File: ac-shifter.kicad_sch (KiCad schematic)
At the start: 11 parts

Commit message: schem: annotate back ac level shifter page
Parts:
- gave numbers to parts that had none: 6
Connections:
- net +10/20DC: now also U10.8 (V+)
- net GND: now also U10.4 (V-)
- net OL: now also U10.7; no longer U10.1
- net Vref: now also U10.6 (-); no longer U10.2 (-)
- net at C32.1, R37.2, R47.1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: now also U10.5 (+); no longer U10.3 (+)
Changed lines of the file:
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@@
 		(dnp no)
 		(fields_autoplaced yes)
-		(property "Reference" "R?"
+		(property "Reference" "R48"
 			(at 184.15 105.4099 0)
 			(effects
@@
 			(project "esp32c6-sensor-devboard"
 				(path "/f6edeef8-7fa0-4f55-9ad8-145372f41e3e/b7a168fa-ef36-46f7-85e2-013385835bc1"
-					(reference "R?")
+					(reference "R48")
 					(unit 1)
 				)
@@
 		(lib_id "Comparator:LM393")
 		(at 128.27 60.96 0)
-		(unit 1)
-		(exclude_from_sim no)
-		(in_bom yes)
-		(on_board yes)
-		(dnp no)
-		(fields_autoplaced yes)
-		(property "Reference" "U?"
+		(unit 3)
+		(exclude_from_sim no)
+		(in_bom yes)
+		(on_board yes)
+		(dnp no)
+		(fields_autoplaced yes)
+		(property "Reference" "U10"
 			(at 127 59.6899 0)
 			(effects
@@
 			(project "esp32c6-sensor-devboard"
 				(path "/f6edeef8-7fa0-4f55-9ad8-145372f41e3e/b7a168fa-ef36-46f7-85e2-013385835bc1"
-					(reference "U?")
-					(unit 1)
+					(reference "U10")
+					(unit 3)
 				)
 			)
@@
 		(on_board yes)
 		(dnp no)
-		(property "Reference" "C?"
+		(property "Reference" "C40"
 			(at 111.76 55.8799 0)
 			(effects
@@
 			(project "esp32c6-sensor-devboard"
 				(path "/f6edeef8-7fa0-4f55-9ad8-145372f41e3e/b7a168fa-ef36-46f7-85e2-013385835bc1"
-					(reference "C?")
+					(reference "C40")
 					(unit 1)
 				)
@@
 		(on_board yes)
 		(dnp no)
-		(property "Reference" "D?"
+		(property "Reference" "D5"
 			(at 99.568 90.424 0)
 			(effects
@@
 			(project "esp32c6-sensor-devboard"
 				(path "/f6edeef8-7fa0-4f55-9ad8-145372f41e3e/b7a168fa-ef36-46f7-85e2-013385835bc1"
-					(reference "D?")
+					(reference "D5")
 					(unit 1)
 				)
@@
 		(dnp no)
 		(fields_autoplaced yes)
-		(property "Reference" "C?"
+		(property "Reference" "C39"
 			(at 113.03 99.0599 0)
 			(effects
@@
 			(project "esp32c6-sensor-devboard"
 				(path "/f6edeef8-7fa0-4f55-9ad8-145372f41e3e/b7a168fa-ef36-46f7-85e2-013385835bc1"
-					(reference "C?")
+					(reference "C39")
 					(unit 1)
 				)
@@
 		(on_board yes)
 		(dnp no)
-		(property "Reference" "U?"
+		(property "Reference" "U10"
 			(at 170.18 68.58 0)
 			(effects
@@
 			(project "esp32c6-sensor-devboard"
 				(path "/f6edeef8-7fa0-4f55-9ad8-145372f41e3e/b7a168fa-ef36-46f7-85e2-013385835bc1"
-					(reference "U?")
+					(reference "U10")
 					(unit 1)
 				)
@@
 		(dnp no)
 		(fields_autoplaced yes)
-		(property "Reference" "R?"
+		(property "Reference" "R47"
 			(at 142.24 99.0599 0)
 			(effects
@@
 			(project "esp32c6-sensor-devboard"
 				(path "/f6edeef8-7fa0-4f55-9ad8-145372f41e3e/b7a168fa-ef36-46f7-85e2-013385835bc1"
-					(reference "R?")
+					(reference "R47")
 					(unit 1)
 				)
@@
 		(lib_id "Comparator:LM393")
 		(at 170.18 114.3 0)
-		(unit 1)
-		(exclude_from_sim no)
-		(in_bom yes)
-		(on_board yes)
-		(dnp no)
-		(fields_autoplaced yes)
-		(property "Reference" "U?"
+		(unit 2)
+		(exclude_from_sim no)
+		(in_bom yes)
+		(on_board yes)
+		(dnp no)
+		(fields_autoplaced yes)
+		(property "Reference" "U10"
 			(at 170.18 104.14 0)
 			(effects
@@
 			(project "esp32c6-sensor-devboard"
 				(path "/f6edeef8-7fa0-4f55-9ad8-145372f41e3e/b7a168fa-ef36-46f7-85e2-013385835bc1"
-					(reference "U?")
-					(unit 1)
-				)
-			)
+					(reference "U10")
+					(unit 2)
+				)
+			)

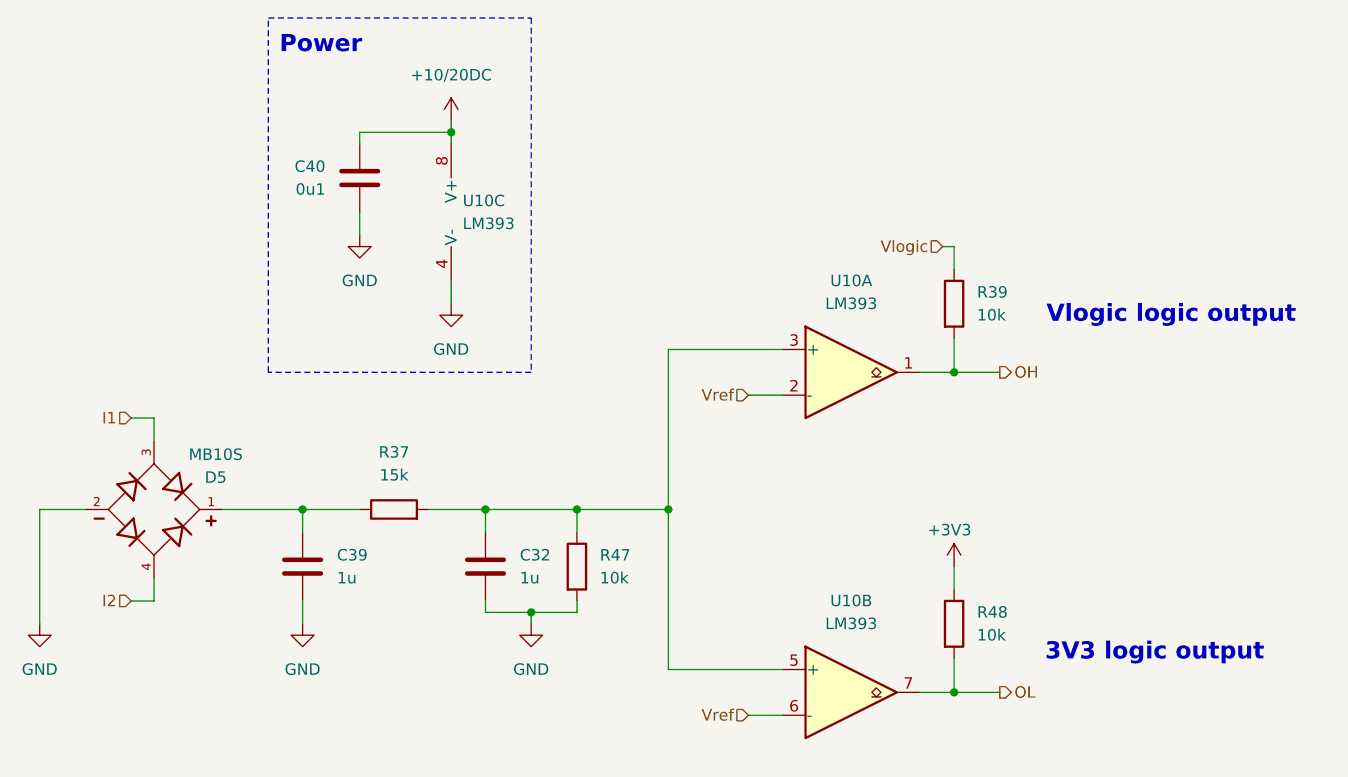
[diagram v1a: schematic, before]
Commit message: schem: add 3CH 24V/12V Input level shifter
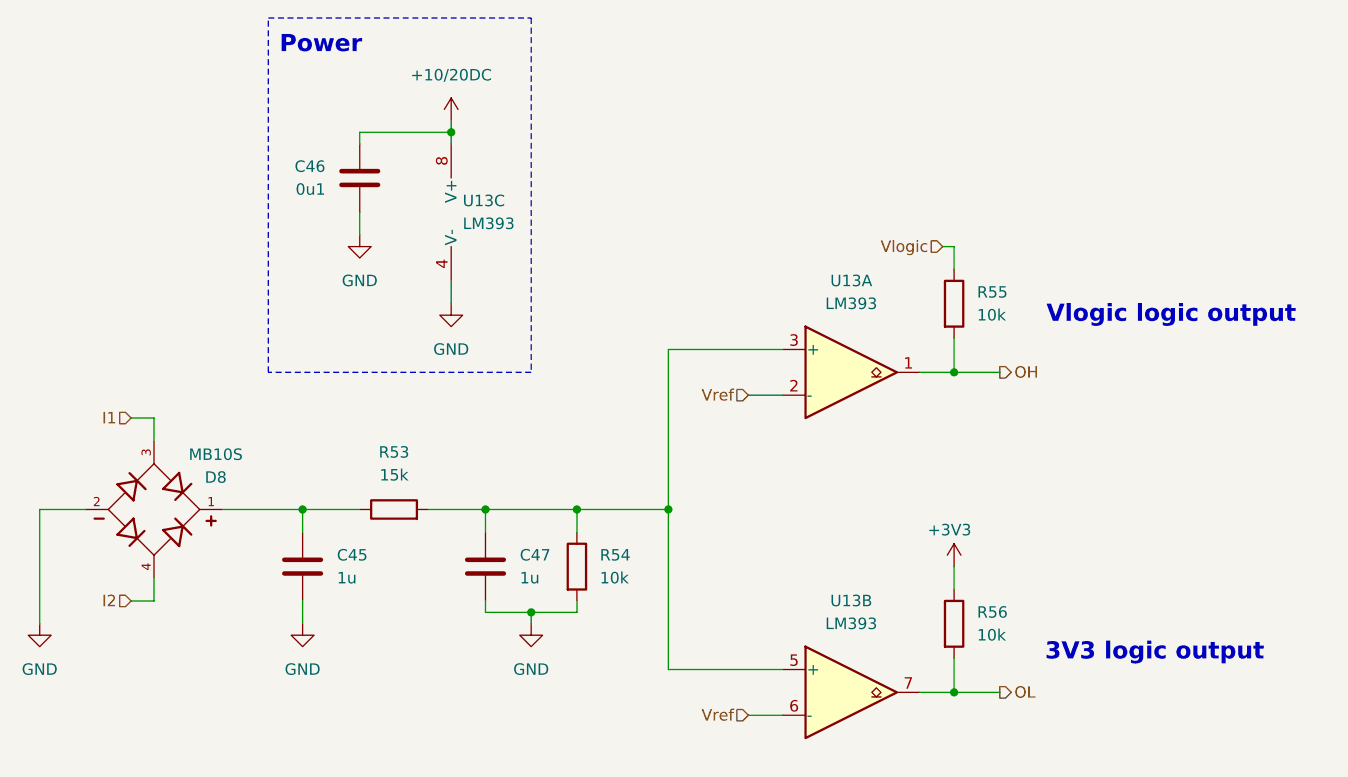
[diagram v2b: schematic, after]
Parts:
- renumbered C39 to C45, C40 to C46, C32 to C47, D5 to D8, R37 to R53, R47 to R54, R39 to R55, R48 to R56, U10 to U13

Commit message: schem: add comparator test points
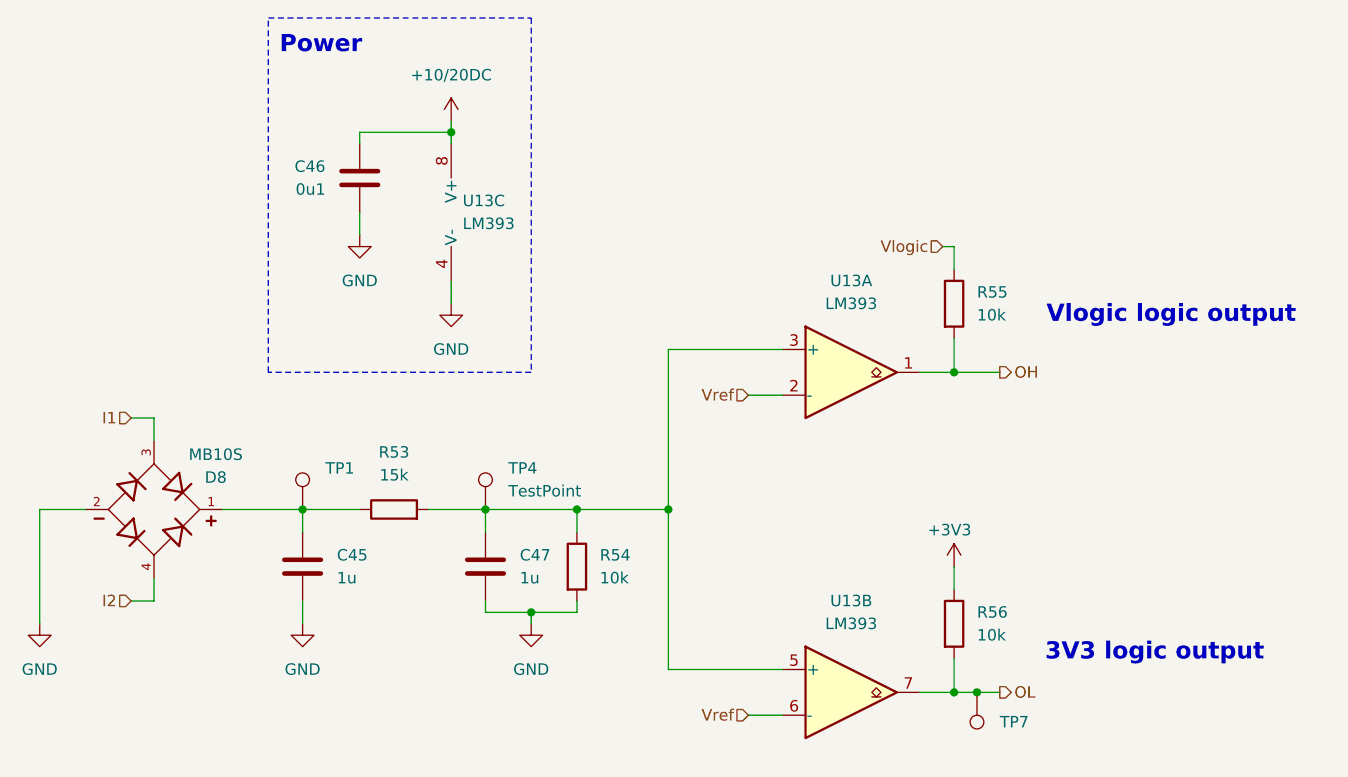
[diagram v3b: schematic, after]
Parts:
- added TP1, TP4, TP7: TestPoint, symbol Connector:TestPoint
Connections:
- net OL: now also TP7.1
- net at C45.1, D8.1, R53.1: now also TP1.1
- net at C47.1, R53.2, R54.1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: now also TP4.1
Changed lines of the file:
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@@
+	)
+	(junction
+		(at 184.15 114.3)
+		(diameter 0)
+		(color 0 0 0 0)
 	)
 	(junction
@@
 	(wire
 		(pts
-			(xy 181.61 114.3) (xy 186.69 114.3)
+			(xy 181.61 114.3) (xy 184.15 114.3)
 		)
 		(stroke
@@
 		(pts
 			(xy 181.61 74.93) (xy 181.61 78.74)
+		)
+		(stroke
+			(width 0)
+			(type default)
+		)
+	)
+	(wire
+		(pts
+			(xy 184.15 114.3) (xy 186.69 114.3)
 		)
 		(stroke
@@
 	)
 	(symbol
+		(lib_id "Connector:TestPoint")
+		(at 129.54 93.98 0)
+		(unit 1)
+		(exclude_from_sim no)
+		(in_bom yes)
+		(on_board yes)
+		(dnp no)
+		(fields_autoplaced yes)
+		(property "Reference" "TP4"
+			(at 132.08 89.4079 0)
+			(effects
+				(font
+					(size 1.27 1.27)
+				)
+				(justify left)
+			)
+		)
+		(property "Value" "TestPoint"
+			(at 132.08 91.9479 0)
+			(effects
+				(font
+					(size 1.27 1.27)
+				)
+				(justify left)
+			)
+		)
+		(property "Footprint" ""
+			(at 134.62 93.98 0)
+			(effects
+				(font
+					(size 1.27 1.27)
+				)
+				(hide yes)
+			)
+		)
+		(property "Datasheet" "~"
+			(at 134.62 93.98 0)
+			(effects
+				(font
+					(size 1.27 1.27)
+				)
+				(hide yes)
+			)
+		)
+		(property "Description" "test point"
+			(at 129.54 93.98 0)
+			(effects
+				(font
+					(size 1.27 1.27)
+				)
+				(hide yes)
+			)
+		)
+		(pin "1"
+		)
+		(instances
+			(project ""
+				(path "/f6edeef8-7fa0-4f55-9ad8-145372f41e3e/30405a70-5ee8-4fa0-855b-2b8bdab4954c"
+					(reference "TP5")
+					(unit 1)
+				)
+				(path "/f6edeef8-7fa0-4f55-9ad8-145372f41e3e/5f6c93b9-e933-4ea9-a357-6909cb7c1eb6"
+					(reference "TP4")
+					(unit 1)
+				)
+				(path "/f6edeef8-7fa0-4f55-9ad8-145372f41e3e/a6afd72b-5a4f-47cb-8cd9-76696d192618"
+					(reference "TP6")
+					(unit 1)
+				)
+			)
+		)
+	)
+	(symbol
 		(lib_id "Device:C")
 		(at 129.54 100.33 0)
@@
 	)
 	(symbol
+		(lib_id "Connector:TestPoint")
+		(at 109.22 93.98 0)
+		(unit 1)
+		(exclude_from_sim no)
+		(in_bom yes)
+		(on_board yes)
+		(dnp no)
+		(fields_autoplaced yes)
+		(property "Reference" "TP1"
+			(at 111.76 89.4079 0)
+			(effects
+				(font
+					(size 1.27 1.27)
+				)
+				(justify left)
+			)
+		)
+		(property "Value" "TestPoint"
+			(at 111.76 91.9479 0)
+			(effects
+				(font
+					(size 1.27 1.27)
+				)
+				(justify left)
+				(hide yes)
+			)
+		)
+		(property "Footprint" ""
+			(at 114.3 93.98 0)
+			(effects
+				(font
+					(size 1.27 1.27)
+				)
+				(hide yes)
+			)
+		)
+		(property "Datasheet" "~"
+			(at 114.3 93.98 0)
+			(effects
+				(font
+					(size 1.27 1.27)
+				)
+				(hide yes)
+			)
+		)
+		(property "Description" "test point"
+			(at 109.22 93.98 0)
+			(effects
+				(font
+					(size 1.27 1.27)
+				)
+				(hide yes)
+			)
+		)
+		(pin "1"
+		)
+		(instances
+			(project ""
+				(path "/f6edeef8-7fa0-4f55-9ad8-145372f41e3e/30405a70-5ee8-4fa0-855b-2b8bdab4954c"
+					(reference "TP2")
+					(unit 1)
+				)
+				(path "/f6edeef8-7fa0-4f55-9ad8-145372f41e3e/5f6c93b9-e933-4ea9-a357-6909cb7c1eb6"
+					(reference "TP1")
+					(unit 1)
+				)
+				(path "/f6edeef8-7fa0-4f55-9ad8-145372f41e3e/a6afd72b-5a4f-47cb-8cd9-76696d192618"
+					(reference "TP3")
+					(unit 1)
+				)
+			)
+		)
+	)
+	(symbol
 		(lib_id "Device:R")
 		(at 181.61 71.12 0)
@@
 				)
 			)
+		)
+	)
+	(symbol
+		(lib_id "Connector:TestPoint")
+		(at 184.15 114.3 180)
+		(unit 1)
+		(exclude_from_sim no)
+		(in_bom yes)
+		(on_board yes)
+		(dnp no)
+		(fields_autoplaced yes)
+		(property "Reference" "TP7"
+			(at 186.69 117.6019 0)
+			(effects
+				(font
+					(size 1.27 1.27)
+				)
+				(justify right)
+			)
+		)
+		(property "Value" "TestPoint"
+			(at 181.61 116.3321 0)
+			(effects
+				(font
+					(size 1.27 1.27)
+				)
+				(justify left)
+				(hide yes)
+			)
+		)
+		(property "Footprint" ""
+			(at 179.07 114.3 0)
+			(effects
+				(font
+					(size 1.27 1.27)
+				)
+				(hide yes)
+			)
+		)
+		(property "Datasheet" "~"
+			(at 179.07 114.3 0)
+			(effects
+				(font
+					(size 1.27 1.27)
+				)
+				(hide yes)
+			)
+		)
+		(property "Description" "test point"
+			(at 184.15 114.3 0)
+			(effects
+				(font
+					(size 1.27 1.27)
+				)
+				(hide yes)
+			)
+		)
+		(pin "1"
+		)
+		(instances
+			(project "esp32c6-sensor-devboard"
+				(path "/f6edeef8-7fa0-4f55-9ad8-145372f41e3e/30405a70-5ee8-4fa0-855b-2b8bdab4954c"
+					(reference "TP8")
+					(unit 1)
+				)
+				(path "/f6edeef8-7fa0-4f55-9ad8-145372f41e3e/5f6c93b9-e933-4ea9-a357-6909cb7c1eb6"
+					(reference "TP7")
+					(unit 1)
+				)
+				(path "/f6edeef8-7fa0-4f55-9ad8-145372f41e3e/a6afd72b-5a4f-47cb-8cd9-76696d192618"
+					(reference "TP9")
+					(unit 1)
+				)
+			)

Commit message: schem: add power test points
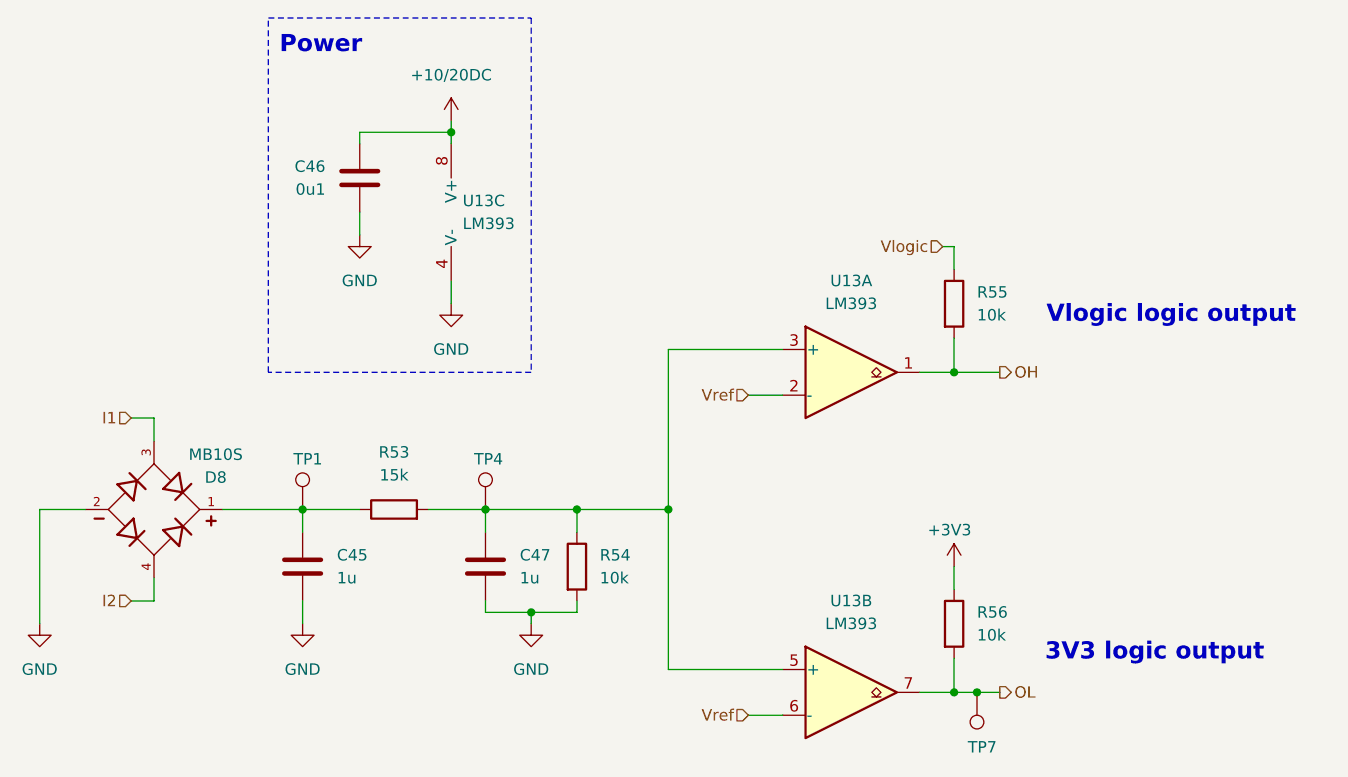
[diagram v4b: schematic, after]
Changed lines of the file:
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@@
 		(on_board yes)
 		(dnp no)
-		(fields_autoplaced yes)
 		(property "Reference" "TP4"
-			(at 132.08 89.4079 0)
+			(at 128.27 88.392 0)
 			(effects
 				(font
@@
 				)
 				(justify left)
+				(hide yes)
 			)
 		)
@@
 		(on_board yes)
 		(dnp no)
-		(fields_autoplaced yes)
 		(property "Reference" "TP1"
-			(at 111.76 89.4079 0)
+			(at 108.204 88.392 0)
 			(effects
 				(font
@@
 		(on_board yes)
 		(dnp no)
-		(fields_autoplaced yes)
 		(property "Reference" "TP7"
-			(at 186.69 117.6019 0)
-			(effects
-				(font
+			(at 183.134 120.396 0)
+			(effects
+				(font

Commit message: schem: add sheet titles
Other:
- company: (none) -> Rémi Ait-Younes
- title: (none) -> AC Level Shifter
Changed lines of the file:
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@@
 	(generator_version "9.0")
 	(paper "A4")
+	(title_block
+		(title "AC Level Shifter")
+		(date "2025-09-26")
+		(rev "01")
+		(company "Rémi Ait-Younes")
+	)
 	(rectangle
 		(start 105.41 39.37)

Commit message: schem: assign footprints
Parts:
- C45: footprint (none) -> Capacitor_SMD:C_0603_1608Metric
- C46, C47: footprint (none) -> Capacitor_SMD:C_0402_1005Metric
- R53, R54, R55, R56: footprint (none) -> Resistor_SMD:R_0603_1608Metric
- TP1, TP4, TP7: footprint (none) -> TestPoint:TestPoint_Pad_D2.0mm
- U13: footprint (none) -> Package_SO:SOIC-8_3.9x4.9mm_P1.27mm
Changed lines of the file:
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@@
 			)
 		)
-		(property "Footprint" ""
+		(property "Footprint" "Resistor_SMD:R_0603_1608Metric"
 			(at 179.832 106.68 90)
 			(effects
@@
 			)
 		)
-		(property "Footprint" ""
+		(property "Footprint" "Resistor_SMD:R_0603_1608Metric"
 			(at 119.38 95.758 90)
 			(effects
@@
 			)
 		)
-		(property "Footprint" ""
+		(property "Footprint" "Package_SO:SOIC-8_3.9x4.9mm_P1.27mm"
 			(at 128.27 60.96 0)
 			(effects
@@
 			)
 		)
-		(property "Footprint" ""
+		(property "Footprint" "Capacitor_SMD:C_0402_1005Metric"
 			(at 116.5352 60.96 0)
 			(effects
@@
 			)
 		)
-		(property "Footprint" ""
+		(property "Footprint" "TestPoint:TestPoint_Pad_D2.0mm"
 			(at 134.62 93.98 0)
 			(effects
@@
 			)
 		)
-		(property "Footprint" ""
+		(property "Footprint" "Capacitor_SMD:C_0402_1005Metric"
 			(at 130.5052 104.14 0)
 			(effects
@@
 			)
 		)
-		(property "Footprint" ""
+		(property "Footprint" "Capacitor_SMD:C_0603_1608Metric"
 			(at 110.1852 104.14 0)
 			(effects
@@
 			)
 		)
-		(property "Footprint" ""
+		(property "Footprint" "Package_SO:SOIC-8_3.9x4.9mm_P1.27mm"
 			(at 170.18 78.74 0)
 			(effects
@@
 			)
 		)
-		(property "Footprint" ""
+		(property "Footprint" "Resistor_SMD:R_0603_1608Metric"
 			(at 137.922 100.33 90)
 			(effects
@@
 			)
 		)
-		(property "Footprint" ""
+		(property "Footprint" "TestPoint:TestPoint_Pad_D2.0mm"
 			(at 114.3 93.98 0)
 			(effects
@@
 			)
 		)
-		(property "Footprint" ""
+		(property "Footprint" "Resistor_SMD:R_0603_1608Metric"
 			(at 179.832 71.12 90)
 			(effects
@@
 			)
 		)
-		(property "Footprint" ""
+		(property "Footprint" "Package_SO:SOIC-8_3.9x4.9mm_P1.27mm"
 			(at 170.18 114.3 0)
 			(effects
@@
 			)
 		)
-		(property "Footprint" ""
+		(property "Footprint" "TestPoint:TestPoint_Pad_D2.0mm"
 			(at 179.07 114.3 0)
 			(effects
